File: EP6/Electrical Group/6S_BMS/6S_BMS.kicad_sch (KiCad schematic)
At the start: 56 parts, among them J1 battery cells, J10 I2C1, J11 CAN1, J12 frontBox, J2 GLVMS, J3 BOOT_BTN, J4 24Vout, J5 CHARGE, J6 UART2, J7 SWD, J8 7seg, J9 RESET, Q1 HSBA3119, Q2 2N7002, Q3 2N7002, Q4 HSBA3119

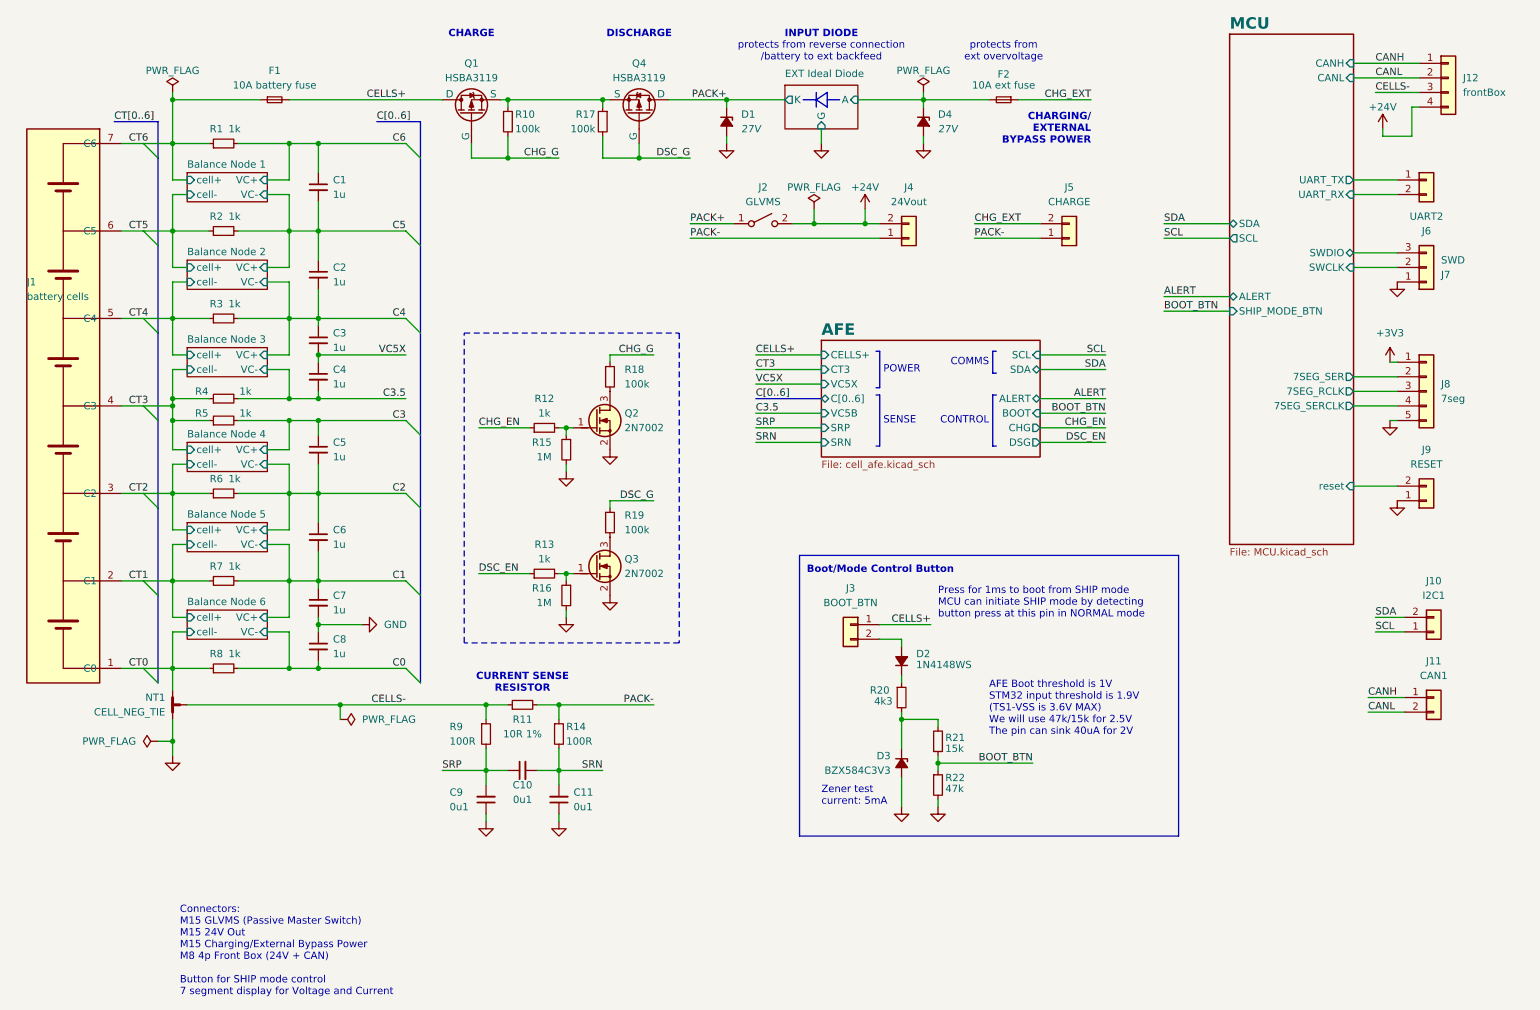
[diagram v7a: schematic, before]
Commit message: front panel board connectors
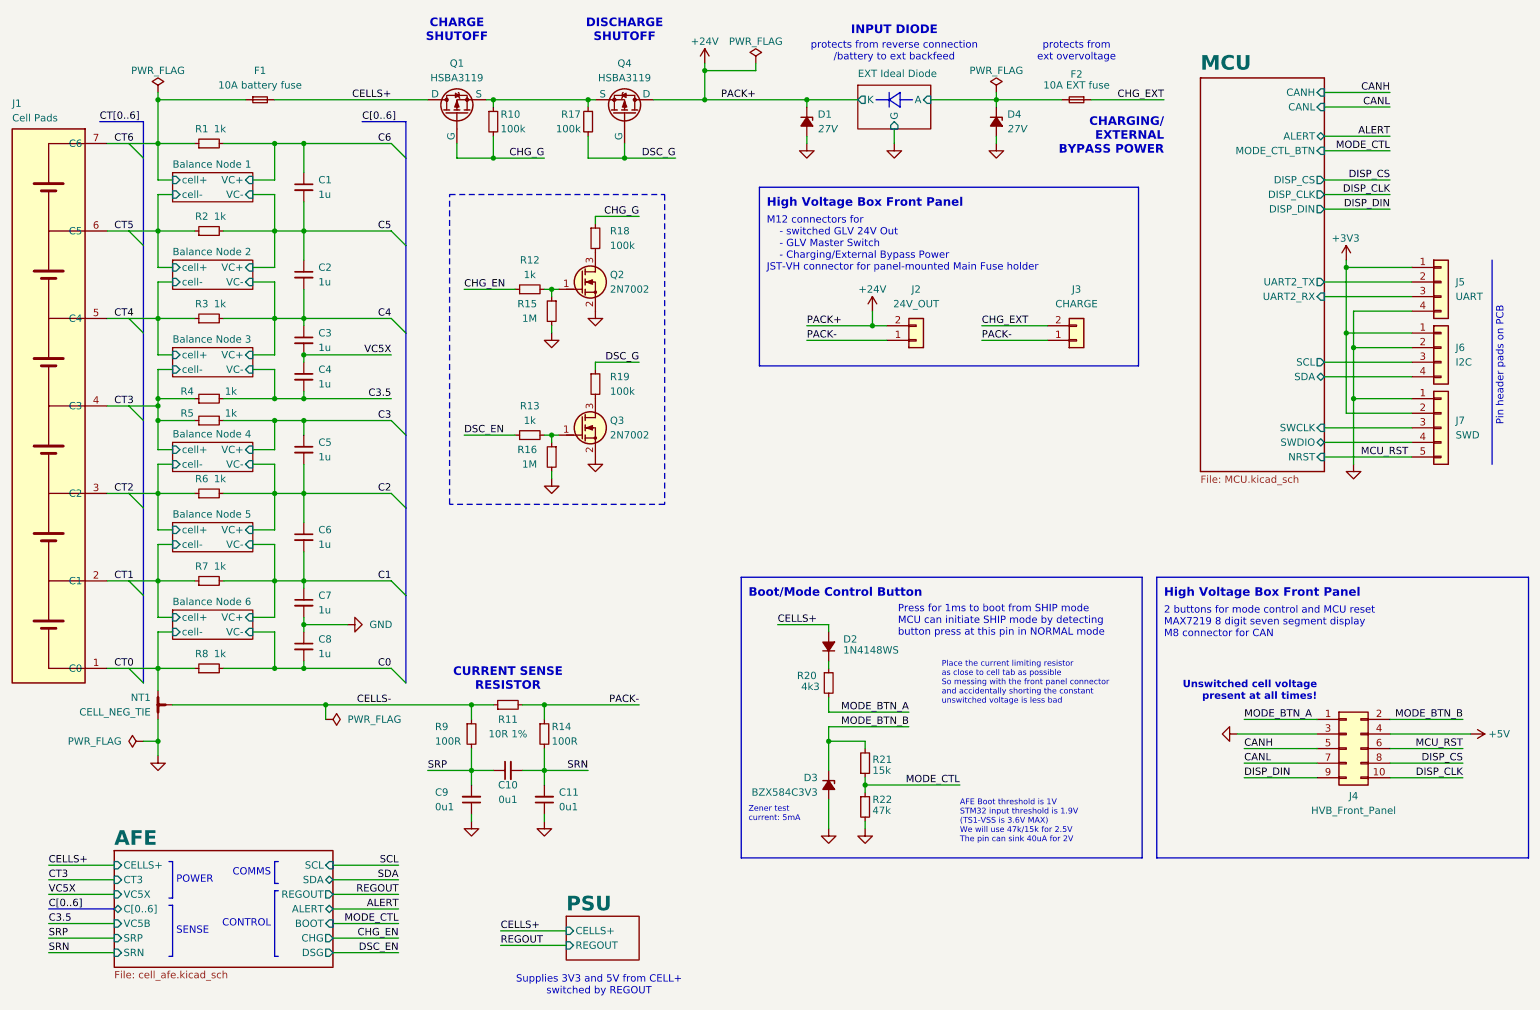
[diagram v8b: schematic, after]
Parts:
- removed J10: I2C1, Connector_JST:JST_PH_S2B-PH-K_1x02_P2.00mm_Horizontal, symbol Connector_Generic:Conn_01x02
- removed J11: CAN1, Connector_JST:JST_PH_S2B-PH-K_1x02_P2.00mm_Horizontal, symbol Connector_Generic:Conn_01x02
- removed J12: frontBox, Connector_JST:JST_PH_S4B-PH-K_1x04_P2.00mm_Horizontal, symbol Connector_Generic:Conn_01x04
- removed J2: GLVMS, Connector_JST:JST_PH_S2B-PH-K_1x02_P2.00mm_Horizontal, symbol Switch:SW_SPST
- removed J3: BOOT_BTN, Connector_JST:JST_PH_S2B-PH-K_1x02_P2.00mm_Horizontal, symbol Connector_Generic:Conn_01x02
- removed J6: UART2, Connector_JST:JST_PH_S2B-PH-K_1x02_P2.00mm_Horizontal, symbol Connector_Generic:Conn_01x02
- removed J7: SWD, Connector_JST:JST_PH_S3B-PH-K_1x03_P2.00mm_Horizontal, symbol Connector_Generic:Conn_01x03
- removed J8: 7seg, Connector_JST:JST_PH_S5B-PH-K_1x05_P2.00mm_Horizontal, symbol Connector_Generic:Conn_01x05
- removed J9: RESET, Connector_JST:JST_PH_S2B-PH-K_1x02_P2.00mm_Horizontal, symbol Connector_Generic:Conn_01x02
- added J4: HVB_Front_Panel, Connector_IDC:IDC-Header_2x05_P2.54mm_Horizontal, symbol Connector_Generic:Conn_02x05_Odd_Even
- added J5: UART, Connector_PinHeader_2.54mm:PinHeader_1x04_P2.54mm_Vertical, symbol Connector_Generic:Conn_01x04
- added J6: I2C, Connector_PinHeader_2.54mm:PinHeader_1x04_P2.54mm_Vertical, symbol Connector_Generic:Conn_01x04
- added J7: SWD, Connector_PinHeader_2.54mm:PinHeader_1x05_P2.54mm_Vertical, symbol Connector_Generic:Conn_01x05
- F1: footprint Fuse:Fuseholder_Cylinder-5x20mm_Schurter_0031_8201_Horizontal_Open -> Fuse:Fuse_1210_3225Metric_Pad1.42x2.65mm_HandSolder
- F2: value 10A ext fuse -> 10A EXT fuse; footprint Fuse:Fuseholder_Cylinder-5x20mm_Schurter_0031_8201_Horizontal_Open -> Fuse:Fuse_1210_3225Metric_Pad1.42x2.65mm_HandSolder
- J1: value battery cells -> Cell Pads
- J2: renamed from J4; value 24Vout -> 24V_OUT; footprint Connector_AMASS:AMASS_XT60PW-F_1x02_P7.20mm_Horizontal -> Connector_JST:JST_VH_B2PS-VH_1x02_P3.96mm_Horizontal
- J3: renamed from J5; footprint Connector_AMASS:AMASS_XT60PW-M_1x02_P7.20mm_Horizontal -> Connector_JST:JST_VH_B2PS-VH_1x02_P3.96mm_Horizontal
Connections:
- net PACK+ is gone; now on net +24V: D1.1 (K), Q4.D
- net +3V3: now also J5.1 (Pin_1), J6.1 (Pin_1), J7.2 (Pin_2)
- net CANH: now also J4.5 (Pin_5)
- net CANL: now also J4.7 (Pin_7)
- net CELLS+: now also D2.2 (A)
- net GND: now also J4.3 (Pin_3), J5.4 (Pin_4), J6.2 (Pin_2), J7.1 (Pin_1)
- net MCU/SWCLK: now also J7.3 (Pin_3)
- net MCU/SWDIO: now also J7.4 (Pin_4)
- net MODE_BTN_B: now reaches D3.1 (K), R21.2
- net MODE_BTN_B: now also J4.2 (Pin_2); no longer R20.2
- net BOOT_BTN renamed MODE_CTL
- new net +5V: J4.4 (Pin_4)
- new net DISP_CLK: J4.10 (Pin_10)
- new net DISP_CS: J4.8 (Pin_8)
- new net DISP_DIN: J4.9 (Pin_9)
- new net MCU/SCL: J6.3 (Pin_3)
- new net MCU/SDA: J6.4 (Pin_4)
- new net MCU/UART2_RX: J5.3 (Pin_3)
- new net MCU/UART2_TX: J5.2 (Pin_2)
- new net MCU_RST: J4.6 (Pin_6), J7.5 (Pin_5)
- new net MODE_BTN_A: J4.1 (Pin_1), R20.2
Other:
- added sheet PSU (psu.kicad_sch)
- sheet AFE ports: added REGOUT; removed none
- sheet MCU ports: added DISP_CLK, DISP_CS, DISP_DIN, MODE_CTL_BTN, NRST, UART2_RX, UART2_TX; removed 7SEG_RCLK, 7SEG_SER, 7SEG_SERCLK, SHIP_MODE_BTN, UART_RX, UART_TX, reset
- note added: "2 buttons for mode control and MCU reset MAX7219 8 digit seven segment display M8 connector for CAN"
- note added: "CHARGE SHUTOFF"
- note added: "DISCHARGE SHUTOFF"
- note added: "High Voltage Box Front Panel"
- note added: "M12 connectors for - switched GLV 24V Out - GLV Master Switch - Charging/External Bypass Power JST-VH connector for panel-mounted Main Fuse holder"
- note added: "Pin header pads on PCB"
- note added: "Place the current limiting resistor as close to cell tab as possible So messing with the front panel connector and accidentally shorting the constant unswitched voltage is less bad"
- note added: "Supplies 3V3 and 5V from CELL+ switched by REGOUT"
- note added: "Unswitched cell voltage present at all times!"
- note removed: "CHARGE"
- note removed: "Connectors: M15 GLVMS (Passive Master Switch) M15 24V Out M15 Charging/External Bypass Power M8 4p Front Box (24V + CAN) Button for SHIP mode control 7 segment display for Voltage and Current"
- note removed: "DISCHARGE"
- moved on the sheet: C1, C10, C11, C2, C3, C4, C5, C6, C7, C8, C9, D1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
